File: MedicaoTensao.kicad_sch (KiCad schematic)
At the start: 14 parts, among them J4 Conn_01x02, J5 Conn_01x02, J6 Conn_01x02, U3 LM324

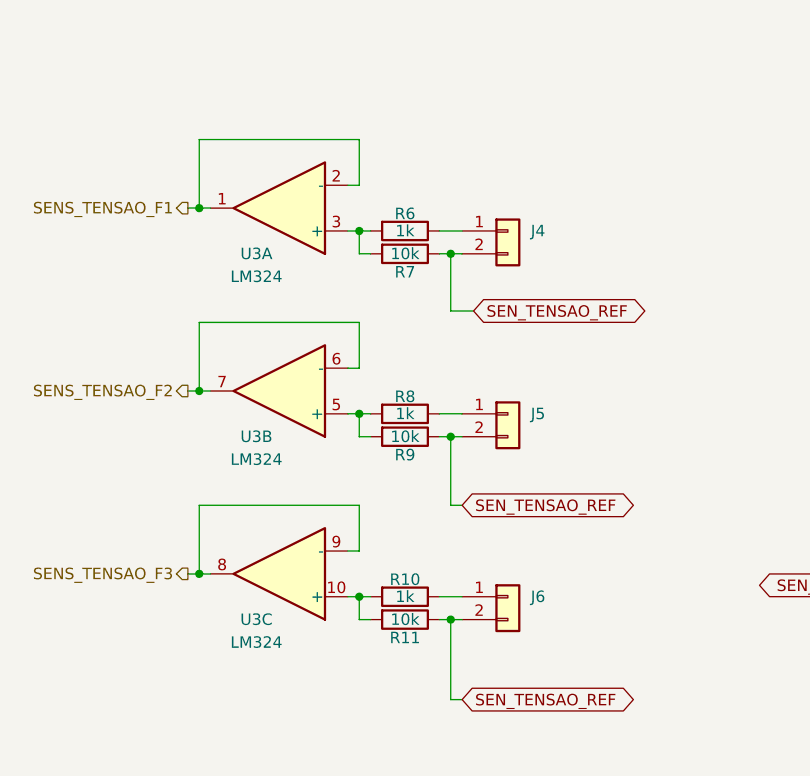
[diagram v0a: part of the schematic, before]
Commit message: Adicionado trimpots para a regulagem da entrada dos sensores de tensão. Adicionou-se também um capacitor de desacolpamento para o ESP32.
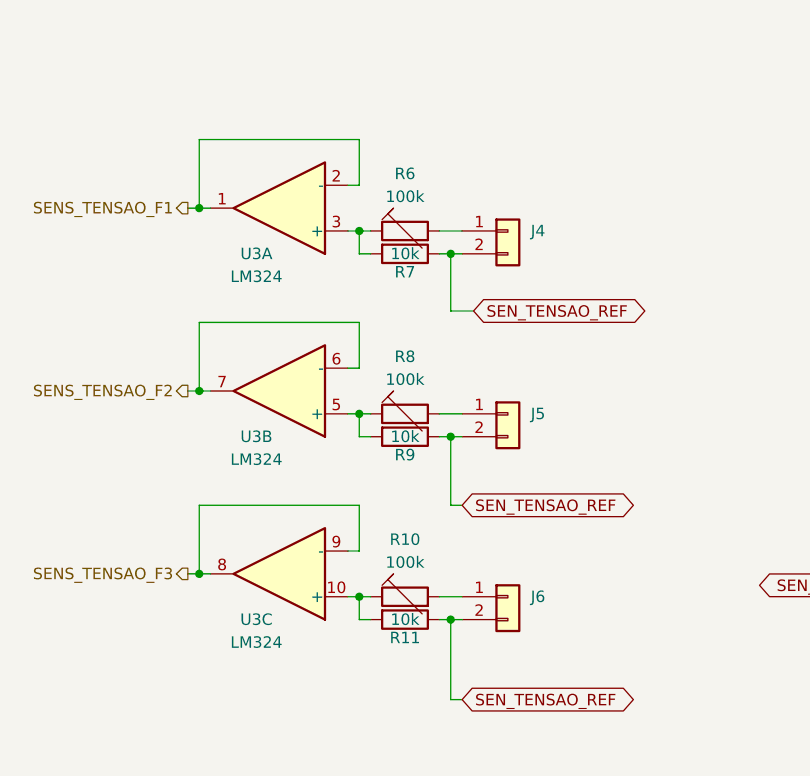
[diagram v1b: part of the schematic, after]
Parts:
- removed R10, R6, R8: 1k, Resistor_THT:R_Axial_DIN0207_L6.3mm_D2.5mm_P10.16mm_Horizontal, symbol Device:R
- added R10, R6, R8: 100k, symbol Device:R_Trim
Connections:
- net at R11.2, U3.10 (+): now also R10.1
- net at J6.1 (Pin_1): now also R10.2
- net at R9.2, U3.5 (+): now also R8.1
- net at R7.2, U3.3 (+): now also R6.1
- net at J4.1 (Pin_1): now also R6.2
- net at J5.1 (Pin_1): now also R8.2
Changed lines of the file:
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@@
     (pin "1")
-  )
-  (symbol (lib_id "Device:R") (at 121.92 120.65 270) (unit 1)
-    (in_bom yes) (on_board yes)
-    (property "Reference" "R10" (id 0) (at 121.92 118.745 90))
-    (property "Value" "1k" (id 1) (at 121.92 120.65 90))
-    (property "Footprint" "Resistor_THT:R_Axial_DIN0207_L6.3mm_D2.5mm_P10.16mm_Horizontal" (id 2) (at 121.92 118.872 90)
-      (effects (font (size 1.27 1.27)) hide)
-    )
-    (property "Datasheet" "~" (id 3) (at 121.92 120.65 0)
-      (effects (font (size 1.27 1.27)) hide)
-    )
-    (pin "1")
-    (pin "2")
   )
   (symbol (lib_id "Amplifier_Operational:LM324") (at 107.95 97.79 180) (unit 2)
@@
     (pin "3")
   )
+  (symbol (lib_id "Device:R_Trim") (at 121.92 120.65 90) (unit 1)
+    (in_bom yes) (on_board yes)
+    (property "Reference" "R10" (id 0) (at 121.92 114.3 90))
+    (property "Value" "100k" (id 1) (at 121.92 116.84 90))
+    (property "Footprint" "" (id 2) (at 121.92 122.428 90)
+      (effects (font (size 1.27 1.27)) hide)
+    )
+    (property "Datasheet" "~" (id 3) (at 121.92 120.65 0)
+      (effects (font (size 1.27 1.27)) hide)
+    )
+    (pin "1")
+    (pin "2")
+  )
   (symbol (lib_id "power:+5V") (at 201.93 72.39 0) (unit 1)
     (in_bom yes) (on_board yes) (fields_autoplaced)
@@
     )
     (pin "1")
-  )
-  (symbol (lib_id "Device:R") (at 121.92 80.01 270) (unit 1)
-    (in_bom yes) (on_board yes)
-    (property "Reference" "R6" (id 0) (at 121.92 78.105 90))
-    (property "Value" "1k" (id 1) (at 121.92 80.01 90))
-    (property "Footprint" "Resistor_THT:R_Axial_DIN0207_L6.3mm_D2.5mm_P10.16mm_Horizontal" (id 2) (at 121.92 78.232 90)
-      (effects (font (size 1.27 1.27)) hide)
-    )
-    (property "Datasheet" "~" (id 3) (at 121.92 80.01 0)
-      (effects (font (size 1.27 1.27)) hide)
-    )
-    (pin "1")
-    (pin "2")
   )
   (symbol (lib_id "Connector_Generic:Conn_01x02") (at 133.35 80.01 0) (unit 1)
@@
     (pin "2")
   )
-  (symbol (lib_id "Device:R") (at 121.92 100.33 270) (unit 1)
-    (in_bom yes) (on_board yes)
-    (property "Reference" "R8" (id 0) (at 121.92 98.425 90))
-    (property "Value" "1k" (id 1) (at 121.92 100.33 90))
-    (property "Footprint" "Resistor_THT:R_Axial_DIN0207_L6.3mm_D2.5mm_P10.16mm_Horizontal" (id 2) (at 121.92 98.552 90)
-      (effects (font (size 1.27 1.27)) hide)
-    )
-    (property "Datasheet" "~" (id 3) (at 121.92 100.33 0)
-      (effects (font (size 1.27 1.27)) hide)
-    )
-    (pin "1")
-    (pin "2")
-  )
   (symbol (lib_id "Device:R") (at 201.93 127 0) (unit 1)
     (in_bom yes) (on_board yes) (fields_autoplaced)
@@
     )
     (property "Datasheet" "~" (id 3) (at 133.35 120.65 0)
+      (effects (font (size 1.27 1.27)) hide)
+    )
+    (pin "1")
+    (pin "2")
+  )
+  (symbol (lib_id "Device:R_Trim") (at 121.92 80.01 90) (unit 1)
+    (in_bom yes) (on_board yes)
+    (property "Reference" "R6" (id 0) (at 121.92 73.66 90))
+    (property "Value" "100k" (id 1) (at 121.92 76.2 90))
+    (property "Footprint" "" (id 2) (at 121.92 81.788 90)
+      (effects (font (size 1.27 1.27)) hide)
+    )
+    (property "Datasheet" "~" (id 3) (at 121.92 80.01 0)
       (effects (font (size 1.27 1.27)) hide)
     )
@@
     (pin "14")
   )
+  (symbol (lib_id "Device:R_Trim") (at 121.92 100.33 90) (unit 1)
+    (in_bom yes) (on_board yes)
+    (property "Reference" "R8" (id 0) (at 121.92 93.98 90))
+    (property "Value" "100k" (id 1) (at 121.92 96.52 90))
+    (property "Footprint" "" (id 2) (at 121.92 102.108 90)
+      (effects (font (size 1.27 1.27)) hide)
+    )
+    (property "Datasheet" "~" (id 3) (at 121.92 100.33 0)
+      (effects (font (size 1.27 1.27)) hide)
+    )
+    (pin "1")
+    (pin "2")
+  )
   (symbol (lib_id "power:GND") (at 201.93 92.71 0) (unit 1)

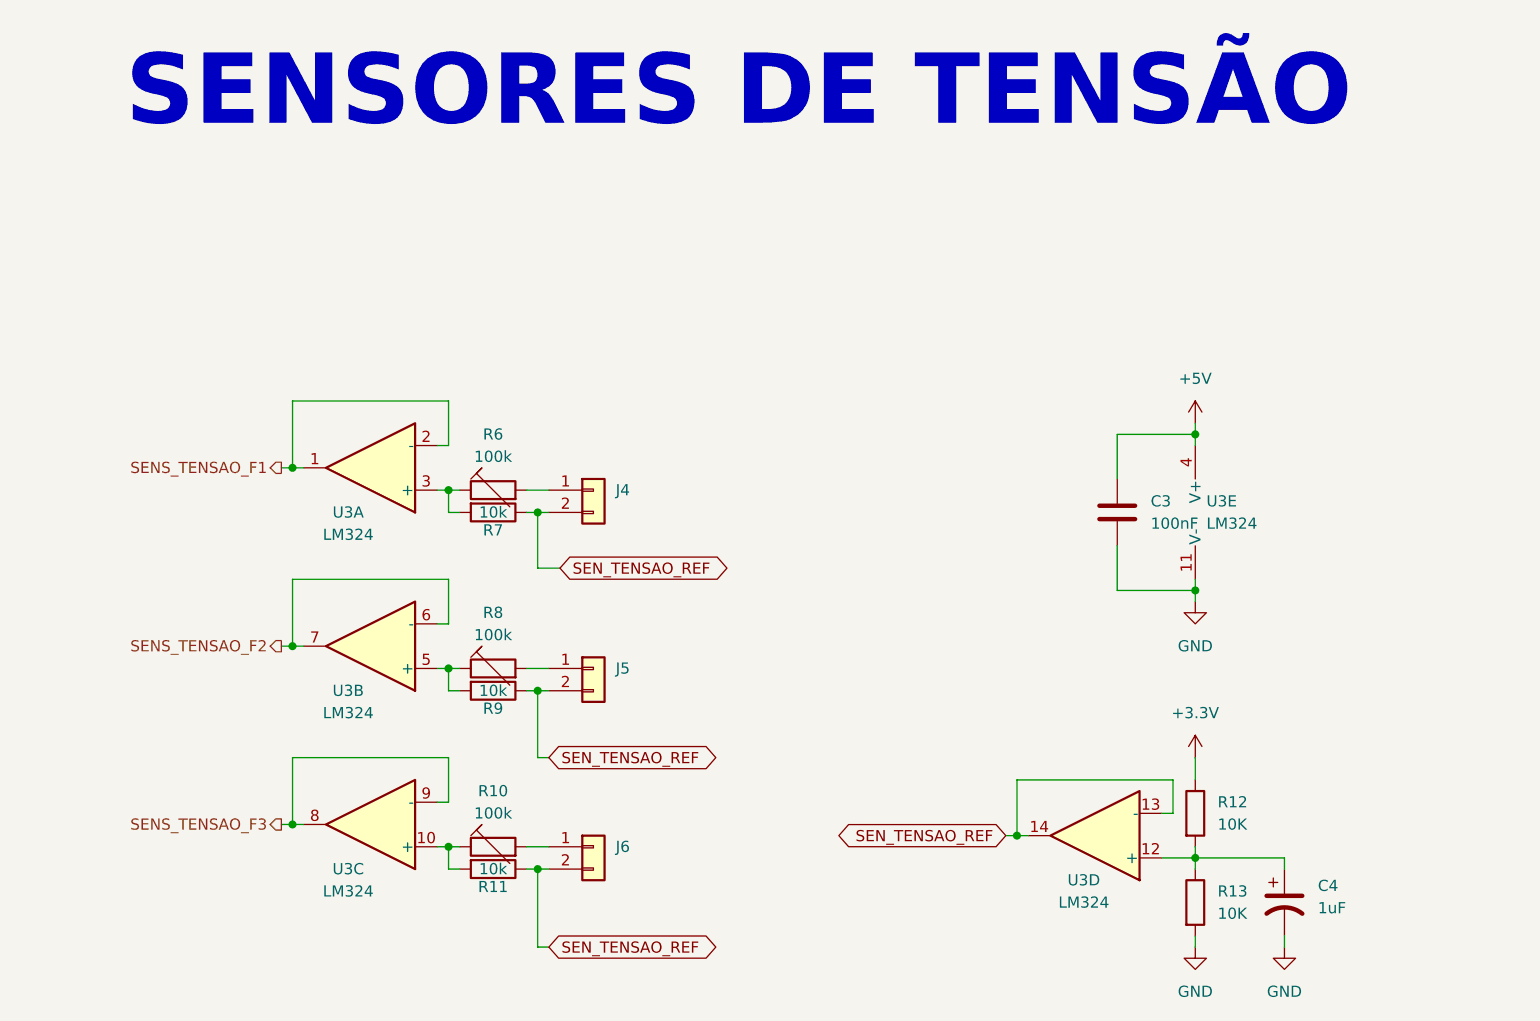
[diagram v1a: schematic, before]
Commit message: Adicionado zeners de proteção para a saída dos buffers
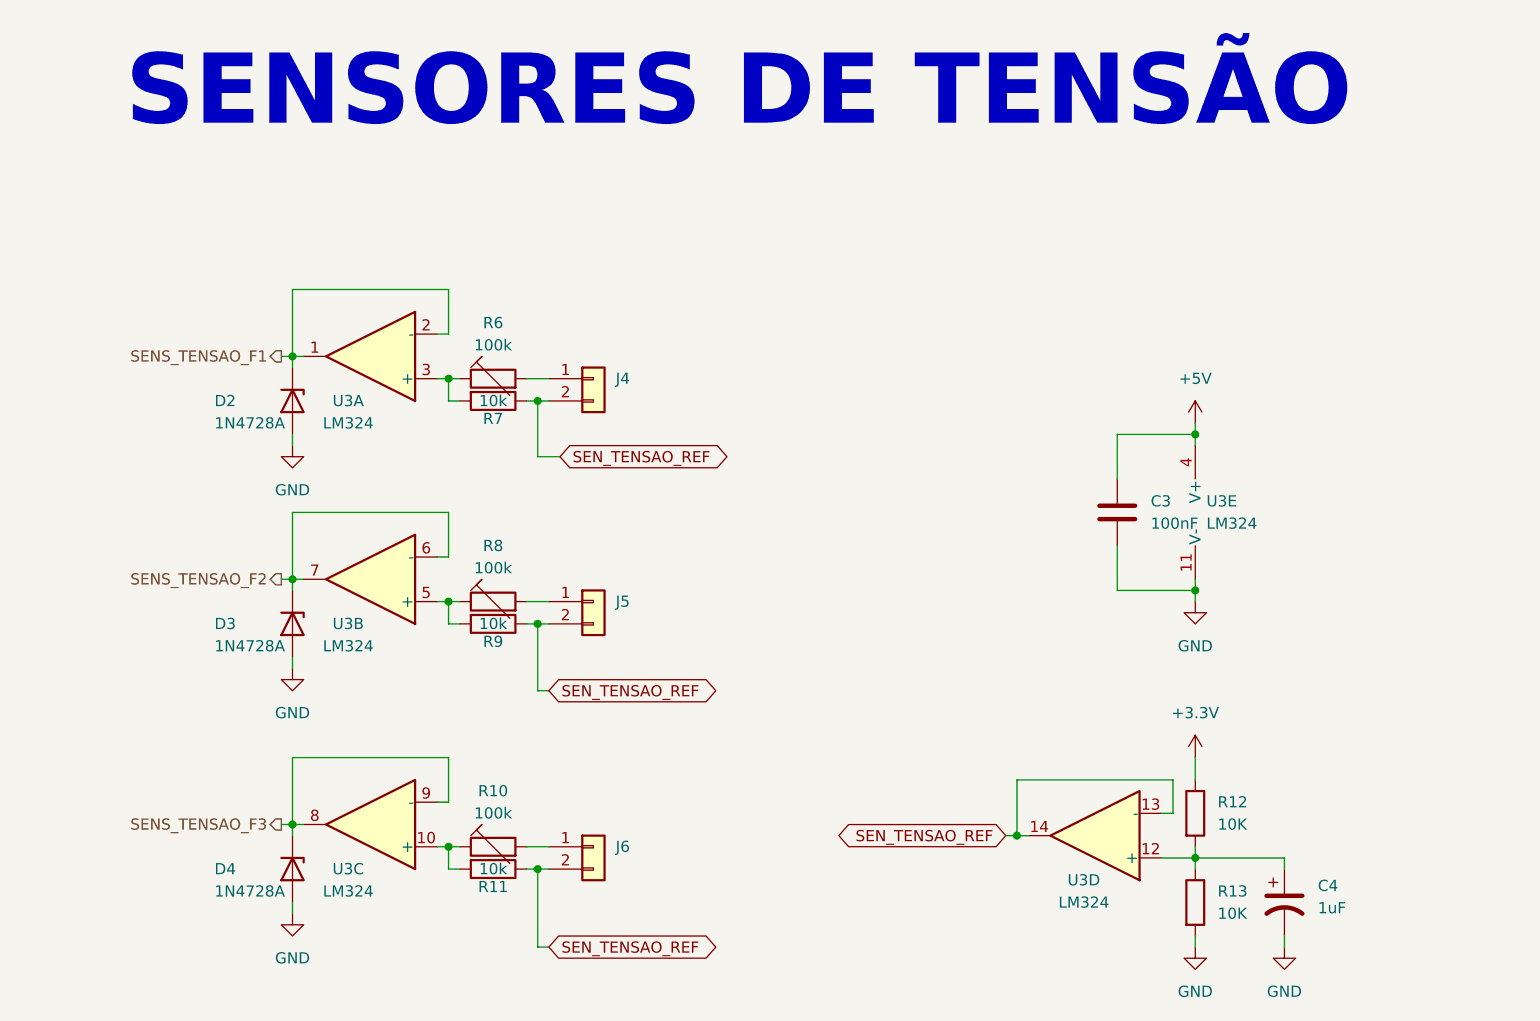
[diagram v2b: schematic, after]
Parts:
- added D2, D3, D4: 1N4728A, Diode_THT:D_DO-41_SOD81_P10.16mm_Horizontal, symbol Diode:1N47xxA
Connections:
- net GND: now also D2.2 (A), D3.2 (A), D4.2 (A)
- net SENS_TENSAO_F1: now also D2.1 (K)
- net SENS_TENSAO_F2: now also D3.1 (K)
- net SENS_TENSAO_F3: now also D4.1 (K)
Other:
- moved on the sheet: J4, J5, R6, R7, R8, R9, U3A, U3B

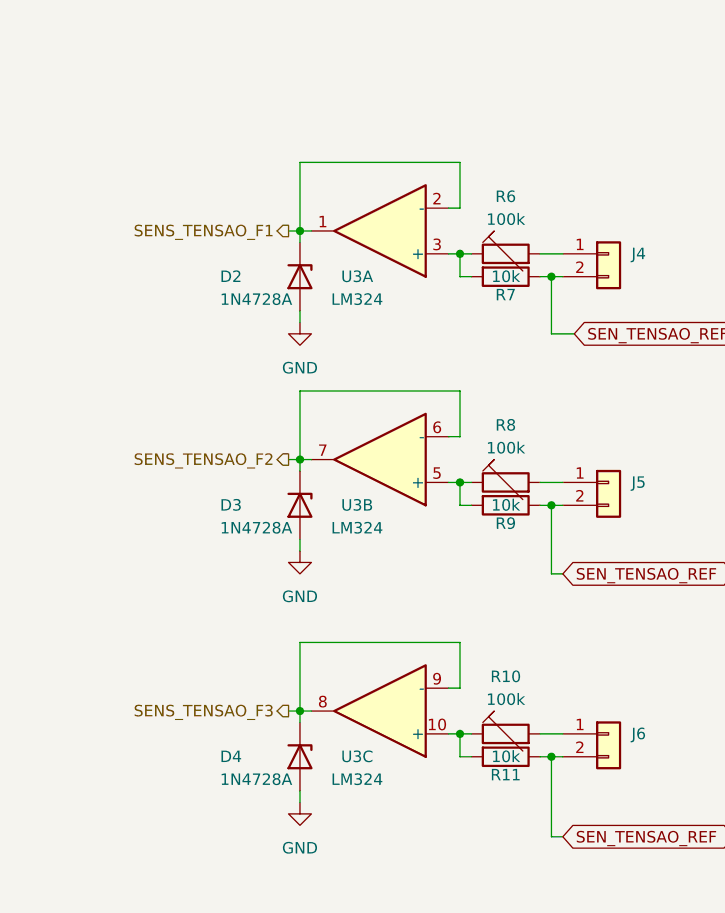
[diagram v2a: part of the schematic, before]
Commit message: As proteções nas saídas dos amplificadores operacionais foram melhoradas e os trimpots foram substituídos por trimpots de 3 pinos, para refletir os que são comprados por aqui.
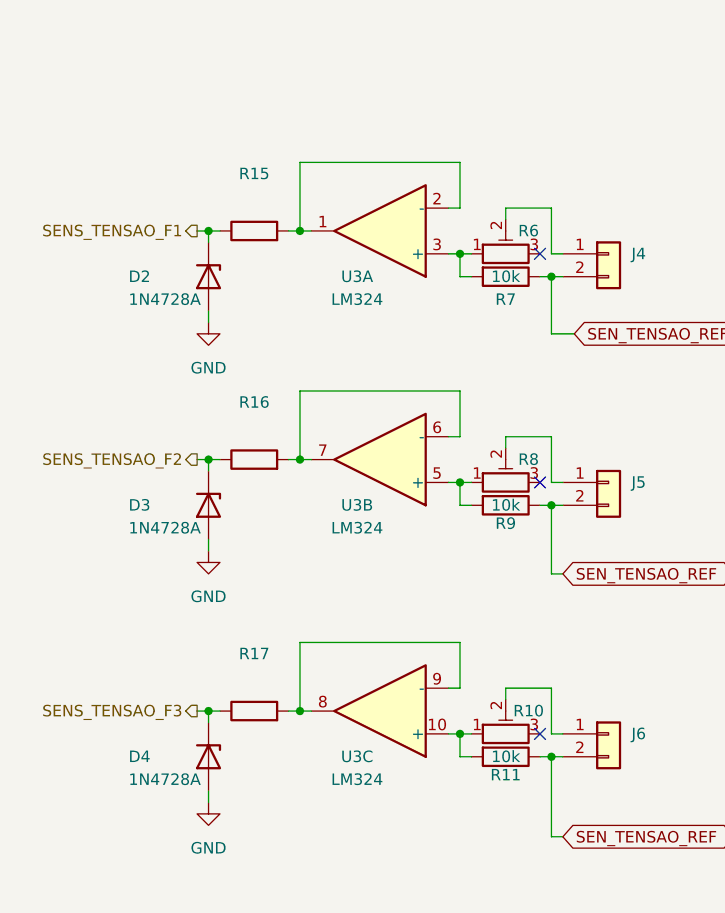
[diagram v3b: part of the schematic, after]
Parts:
- removed R10, R6, R8: 100k, symbol Device:R_Trim
- added R10, R6, R8: (no value), symbol Device:R_Potentiometer_Trim
- added R15, R16, R17: (no value), symbol Device:R
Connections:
- net SENS_TENSAO_F1: now also R15.1; no longer U3.1, U3.2 (-)
- net SENS_TENSAO_F2: now also R16.1; no longer U3.6 (-), U3.7
- net SENS_TENSAO_F3: now also R17.1; no longer U3.8, U3.9 (-)
- net at R11.2, U3.10 (+): now also R10.1
- net at R9.2, U3.5 (+): now also R8.1
- net at R7.2, U3.3 (+): now also R6.1
- net at J6.1 (Pin_1): now also R10.2
- net at J4.1 (Pin_1): now also R6.2
- net at J5.1 (Pin_1): now also R8.2
- new net: R17.2, U3.8, U3.9 (-)
- new net: R16.2, U3.6 (-), U3.7
- new net: R15.2, U3.1, U3.2 (-)
- no-connect marks 0 -> 3
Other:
- moved on the sheet: D2, D3, D4

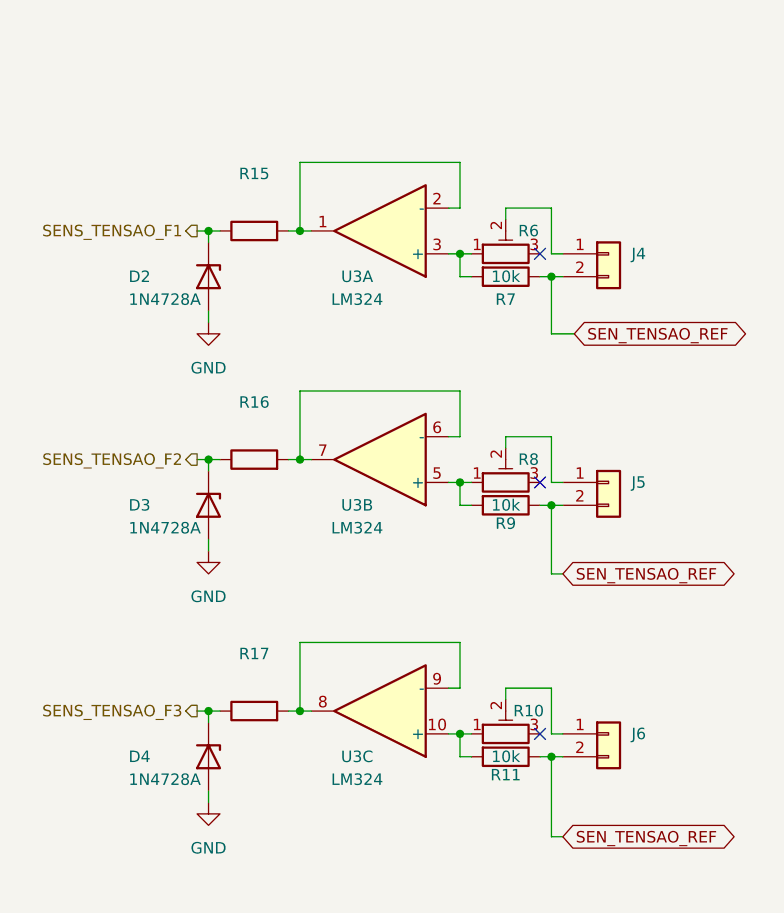
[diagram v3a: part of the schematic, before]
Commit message: Definido todos os footprints para os componentes e feito o DRC
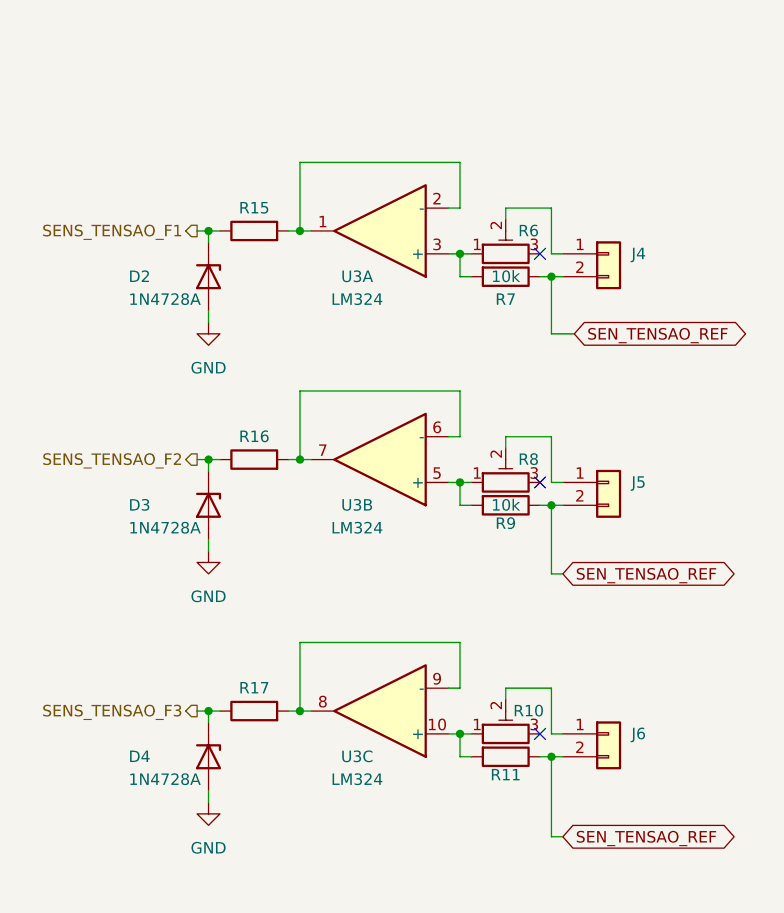
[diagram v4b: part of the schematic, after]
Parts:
- R11: value 10k -> (none); footprint Resistor_THT:R_Axial_DIN0207_L6.3mm_D2.5mm_P10.16mm_Horizontal -> (none)
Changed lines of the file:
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@@
     (in_bom yes) (on_board yes)
     (property "Reference" "R11" (id 0) (at 121.92 125.222 90))
-    (property "Value" "10k" (id 1) (at 121.92 123.19 90))
-    (property "Footprint" "Resistor_THT:R_Axial_DIN0207_L6.3mm_D2.5mm_P10.16mm_Horizontal" (id 2) (at 121.92 121.412 90)
+    (property "Value" "" (id 1) (at 121.92 123.19 90))
+    (property "Footprint" "" (id 2) (at 121.92 121.412 90)
       (effects (font (size 1.27 1.27)) hide)
     )
@@
   )
   (symbol (lib_id "Device:R") (at 93.98 90.17 90) (unit 1)
-    (in_bom yes) (on_board yes) (fields_autoplaced)
-    (property "Reference" "R16" (id 0) (at 93.98 83.82 90))
-    (property "Value" "" (id 1) (at 93.98 86.36 90))
+    (in_bom yes) (on_board yes)
+    (property "Reference" "R16" (id 0) (at 93.98 87.63 90))
+    (property "Value" "" (id 1) (at 93.98 90.17 90))
     (property "Footprint" "" (id 2) (at 93.98 91.948 90)
       (effects (font (size 1.27 1.27)) hide)
@@
   )
   (symbol (lib_id "Device:R") (at 93.98 118.11 90) (unit 1)
-    (in_bom yes) (on_board yes) (fields_autoplaced)
-    (property "Reference" "R17" (id 0) (at 93.98 111.76 90))
-    (property "Value" "" (id 1) (at 93.98 114.3 90))
+    (in_bom yes) (on_board yes)
+    (property "Reference" "R17" (id 0) (at 93.98 115.57 90))
+    (property "Value" "" (id 1) (at 93.98 118.11 90))
     (property "Footprint" "" (id 2) (at 93.98 119.888 90)
       (effects (font (size 1.27 1.27)) hide)
@@
   )
   (symbol (lib_id "Device:R") (at 93.98 64.77 90) (unit 1)
-    (in_bom yes) (on_board yes) (fields_autoplaced)
-    (property "Reference" "R15" (id 0) (at 93.98 58.42 90))
-    (property "Value" "" (id 1) (at 93.98 60.96 90))
+    (in_bom yes) (on_board yes)
+    (property "Reference" "R15" (id 0) (at 93.98 62.23 90))
+    (property "Value" "" (id 1) (at 93.98 64.77 90))
     (property "Footprint" "" (id 2) (at 93.98 66.548 90)
       (effects (font (size 1.27 1.27)) hide)
